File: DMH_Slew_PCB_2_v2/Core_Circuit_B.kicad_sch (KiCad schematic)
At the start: 52 parts, among them J6 TS_Jack_6.35mm_Sw, J60 Conn_01x08_PinHeader, J61 Conn_01x08_PinHeader, J7 TS_Jack_6.35mm_Sw, J8 TS_Jack_6.35mm_Sw, Q10 BC558, Q7 BC548, Q8 BC548, Q9 BC558, SW4 SW_DPDT_3way, SW5 SW_DPDT, SW6 SPDT_OnOffOn, U3 TL074, U4 TL074

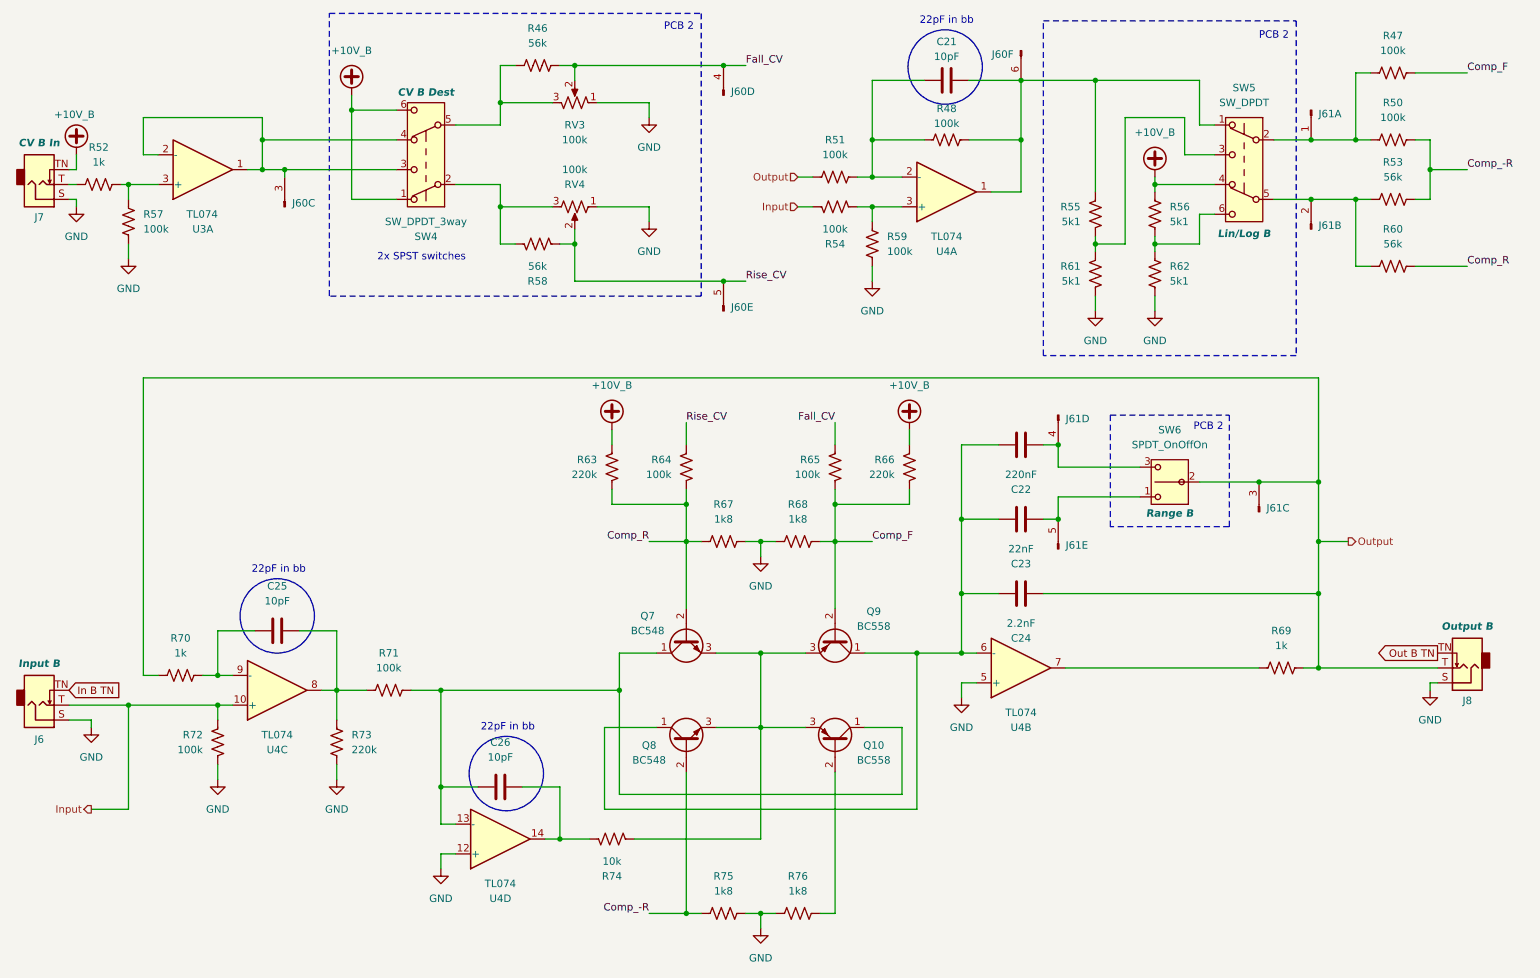
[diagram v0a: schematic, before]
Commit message: PCB 2 component placement done
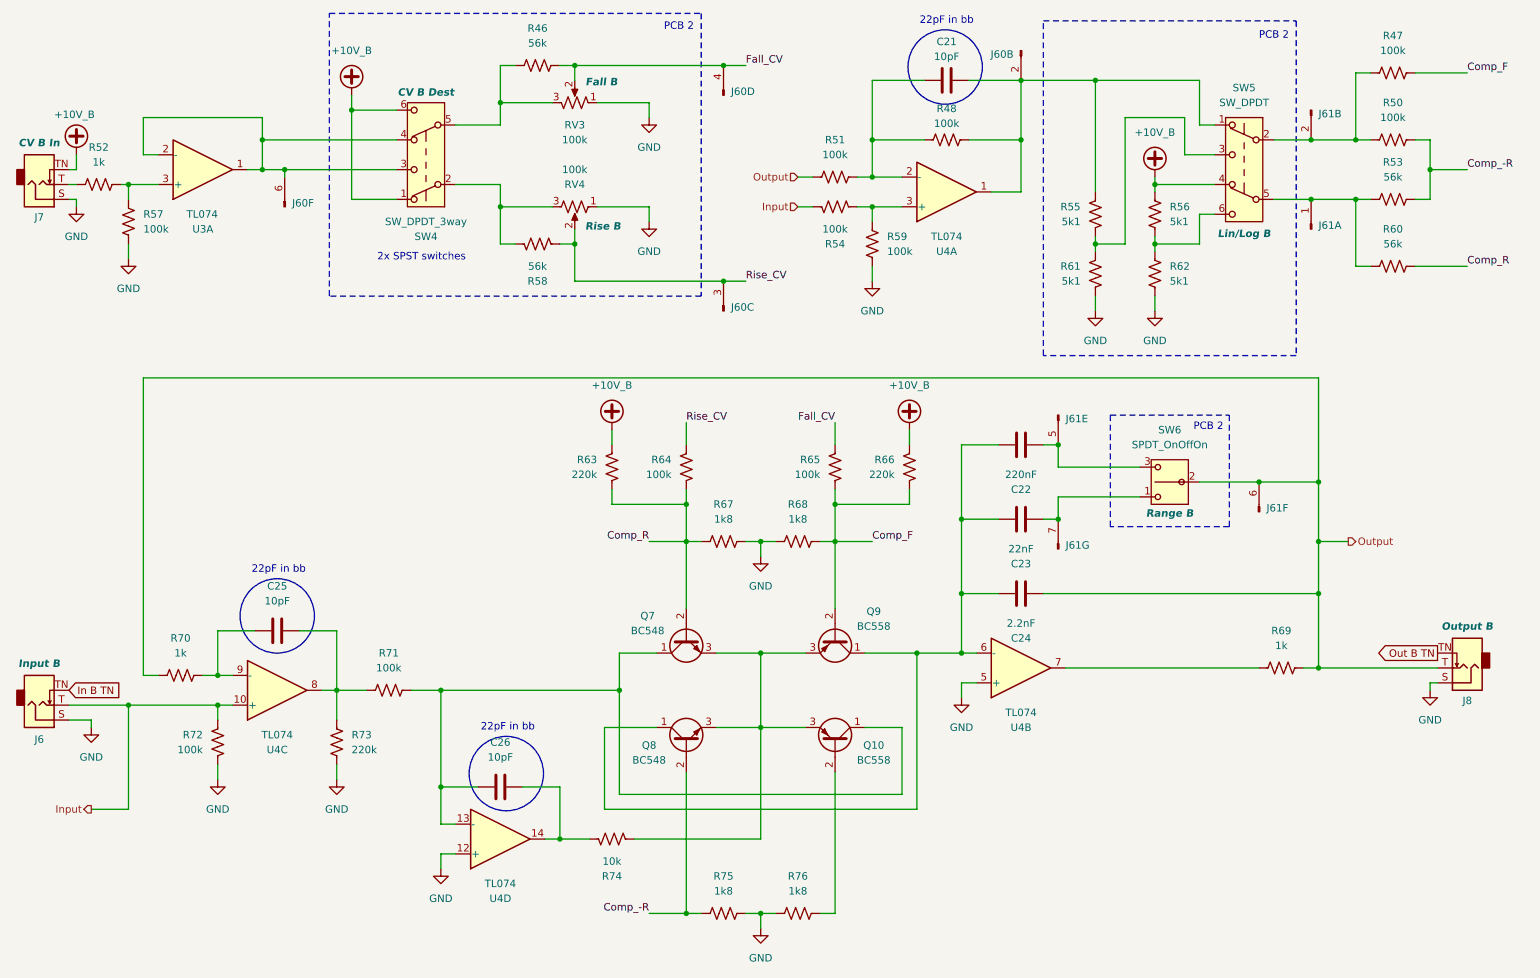
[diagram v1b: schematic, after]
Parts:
- J60, J61: footprint Connector_PinHeader_2.54mm:PinHeader_1x08_P2.54mm_Vertical -> Connector_PinSocket_2.54mm:PinSocket_1x08_P2.54mm_Vertical
- RV3: Function (none) -> Fall B
- RV4: Function (none) -> Rise B
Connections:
- net Output: now also J61.6 (Pin_6); no longer J61.3 (Pin_3)
- net Rise_CV: now also J60.3 (Pin_3); no longer J60.5 (Pin_5)
- net at C21.2, R48.1, R55.1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: now also J60.2 (Pin_2); no longer J60.6 (Pin_6)
- net at C22.2, SW6.3 (C): now also J61.5 (Pin_5); no longer J61.4 (Pin_4)
- net at R53.2, R60.2, SW5.5 (B): now also J61.1 (Pin_1); no longer J61.2 (Pin_2)
- net at SW4.3 (C), SW4.4 (A), U3.1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: now also J60.6 (Pin_6); no longer J60.3 (Pin_3)
- net at R47.2, R50.2, SW5.2 (B): now also J61.2 (Pin_2); no longer J61.1 (Pin_1)
- net at C23.2, SW6.1 (A): now also J61.7 (Pin_7); no longer J61.5 (Pin_5)
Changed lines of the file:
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@@
 		(at 190.5 30.48 90)
 		(mirror x)
-		(unit 6)
+		(unit 2)
 		(exclude_from_sim no)
 		(in_bom yes)
@@
 			)
 		)
-		(property "Footprint" "Connector_PinHeader_2.54mm:PinHeader_1x08_P2.54mm_Vertical"
+		(property "Footprint" "Connector_PinSocket_2.54mm:PinSocket_1x08_P2.54mm_Vertical"
 			(at 190.5 30.48 0)
 			(effects
@@
 				(path "/58f4306d-5387-4983-bb08-41a2313fd315/77d402a4-d1d6-4e9c-af86-3ca5793147b8"
 					(reference "J60")
-					(unit 6)
+					(unit 2)
 				)
 			)
@@
 			)
 		)
-		(property "Footprint" "Connector_PinHeader_2.54mm:PinHeader_1x08_P2.54mm_Vertical"
+		(property "Footprint" "Connector_PinSocket_2.54mm:PinSocket_1x08_P2.54mm_Vertical"
 			(at 139.7 38.1 0)
 			(effects
@@
 		(lib_id "SynthStuff:Conn_01x08_PinHeader")
 		(at 240.03 60.96 90)
-		(unit 2)
+		(unit 1)
 		(exclude_from_sim no)
 		(in_bom yes)
@@
 			)
 		)
-		(property "Footprint" "Connector_PinHeader_2.54mm:PinHeader_1x08_P2.54mm_Vertical"
+		(property "Footprint" "Connector_PinSocket_2.54mm:PinSocket_1x08_P2.54mm_Vertical"
 			(at 240.03 60.96 0)
 			(effects
@@
 				(path "/58f4306d-5387-4983-bb08-41a2313fd315/77d402a4-d1d6-4e9c-af86-3ca5793147b8"
 					(reference "J61")
-					(unit 2)
+					(unit 1)
 				)
 			)
@@
 			)
 		)
-		(property "Function" ""
-			(at 114.3 39.37 0)
+		(property "Function" "Fall B"
+			(at 118.872 35.814 90)
 			(effects
 				(font
 					(size 1.27 1.27)
+					(thickness 0.254)
+					(bold yes)
+					(italic yes)
 				)
 			)
@@
 		(lib_id "SynthStuff:Conn_01x08_PinHeader")
 		(at 231.14 109.22 90)
-		(unit 3)
+		(unit 6)
 		(exclude_from_sim no)
 		(in_bom yes)
@@
 			)
 		)
-		(property "Footprint" "Connector_PinHeader_2.54mm:PinHeader_1x08_P2.54mm_Vertical"
+		(property "Footprint" "Connector_PinSocket_2.54mm:PinSocket_1x08_P2.54mm_Vertical"
 			(at 231.14 109.22 0)
 			(effects
@@
 				(path "/58f4306d-5387-4983-bb08-41a2313fd315/77d402a4-d1d6-4e9c-af86-3ca5793147b8"
 					(reference "J61")
-					(unit 3)
+					(unit 6)
 				)
 			)
@@
 		(lib_id "SynthStuff:Conn_01x08_PinHeader")
 		(at 196.85 115.57 90)
-		(unit 5)
+		(unit 7)
 		(exclude_from_sim no)
 		(in_bom yes)
@@
 			)
 		)
-		(property "Footprint" "Connector_PinHeader_2.54mm:PinHeader_1x08_P2.54mm_Vertical"
+		(property "Footprint" "Connector_PinSocket_2.54mm:PinSocket_1x08_P2.54mm_Vertical"
 			(at 196.85 115.57 0)
 			(effects
@@
 				(path "/58f4306d-5387-4983-bb08-41a2313fd315/77d402a4-d1d6-4e9c-af86-3ca5793147b8"
 					(reference "J61")
-					(unit 5)
+					(unit 7)
 				)
 			)
@@
 		(lib_id "SynthStuff:Conn_01x08_PinHeader")
 		(at 64.77 57.15 90)
-		(unit 3)
+		(unit 6)
 		(exclude_from_sim no)
 		(in_bom yes)
@@
 			)
 		)
-		(property "Footprint" "Connector_PinHeader_2.54mm:PinHeader_1x08_P2.54mm_Vertical"
+		(property "Footprint" "Connector_PinSocket_2.54mm:PinSocket_1x08_P2.54mm_Vertical"
 			(at 64.77 57.15 0)
 			(effects
@@
 				(path "/58f4306d-5387-4983-bb08-41a2313fd315/77d402a4-d1d6-4e9c-af86-3ca5793147b8"
 					(reference "J60")
-					(unit 3)
+					(unit 6)
 				)
 			)
@@
 		(lib_id "SynthStuff:Conn_01x08_PinHeader")
 		(at 196.85 92.71 270)
-		(unit 4)
+		(unit 5)
 		(exclude_from_sim no)
 		(in_bom yes)
@@
 			)
 		)
-		(property "Footprint" "Connector_PinHeader_2.54mm:PinHeader_1x08_P2.54mm_Vertical"
+		(property "Footprint" "Connector_PinSocket_2.54mm:PinSocket_1x08_P2.54mm_Vertical"
 			(at 196.85 92.71 0)
 			(effects
@@
 				(path "/58f4306d-5387-4983-bb08-41a2313fd315/77d402a4-d1d6-4e9c-af86-3ca5793147b8"
 					(reference "J61")
-					(unit 4)
+					(unit 5)
 				)
 			)
@@
 		(lib_id "SynthStuff:Conn_01x08_PinHeader")
 		(at 240.03 40.64 270)
-		(unit 1)
+		(unit 2)
 		(exclude_from_sim no)
 		(in_bom yes)
@@
 			)
 		)
-		(property "Footprint" "Connector_PinHeader_2.54mm:PinHeader_1x08_P2.54mm_Vertical"
+		(property "Footprint" "Connector_PinSocket_2.54mm:PinSocket_1x08_P2.54mm_Vertical"
 			(at 240.03 40.64 0)
 			(effects
@@
 				(path "/58f4306d-5387-4983-bb08-41a2313fd315/77d402a4-d1d6-4e9c-af86-3ca5793147b8"
 					(reference "J61")
-					(unit 1)
+					(unit 2)
 				)
 			)
@@
 		(lib_id "SynthStuff:Conn_01x08_PinHeader")
 		(at 139.7 74.93 90)
-		(unit 5)
+		(unit 3)
 		(exclude_from_sim no)
 		(in_bom yes)
@@
 			)
 		)
-		(property "Footprint" "Connector_PinHeader_2.54mm:PinHeader_1x08_P2.54mm_Vertical"
+		(property "Footprint" "Connector_PinSocket_2.54mm:PinSocket_1x08_P2.54mm_Vertical"
 			(at 139.7 74.93 0)
 			(effects
@@
 				(path "/58f4306d-5387-4983-bb08-41a2313fd315/77d402a4-d1d6-4e9c-af86-3ca5793147b8"
 					(reference "J60")
-					(unit 5)
+					(unit 3)
 				)
 			)
@@
 			)
 		)
-		(property "Function" ""
-			(at 114.3 57.15 0)
+		(property "Function" "Rise B"
+			(at 119.126 60.452 90)
 			(effects
 				(font
 					(size 1.27 1.27)
+					(thickness 0.254)
+					(bold yes)
+					(italic yes)
 				)
 			)

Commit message: Updated Log circuit
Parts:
- removed R55, R56, R61, R62: 5k1, Resistor_THT:R_Axial_DIN0207_L6.3mm_D2.5mm_P7.62mm_Horizontal, symbol Device:R_US
- R53, R60: value 56k -> 100k
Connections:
- net GND: now also SW5.3 (C), SW5.6 (C)
